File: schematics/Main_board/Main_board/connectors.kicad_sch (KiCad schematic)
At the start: 13 parts, among them J1 USB_B_Micro, J2 Conn_01x16_Female

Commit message: fix: 3d step file paths
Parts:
- D2, D3, D4: footprint Resistor_SMD:R_0603_1608Metric -> Resistor_SMD:R_0402_1005Metric
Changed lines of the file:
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@@
       (effects (font (size 1.27 1.27)) (justify left) hide)
     )
-    (property "Footprint" "Resistor_SMD:R_0603_1608Metric" (at 46.99 110.49 0)
+    (property "Footprint" "Resistor_SMD:R_0402_1005Metric" (at 46.99 110.49 0)
       (effects (font (size 1.27 1.27)) hide)
     )
@@
       (effects (font (size 1.27 1.27)) (justify left) hide)
     )
-    (property "Footprint" "Resistor_SMD:R_0603_1608Metric" (at 50.8 110.49 0)
+    (property "Footprint" "Resistor_SMD:R_0402_1005Metric" (at 50.8 110.49 0)
       (effects (font (size 1.27 1.27)) hide)
     )
@@
       (effects (font (size 1.27 1.27)) (justify left) hide)
     )
-    (property "Footprint" "Resistor_SMD:R_0603_1608Metric" (at 54.61 110.49 0)
-      (effects (font (size 1.27 1.27)) hide)
-    )
+    (property "Footprint" "Resistor_SMD:R_0402_1005Metric" (at 54.61 110.49 0)
+      (effects (font (size 1.27 1.27)) hide)
+    )

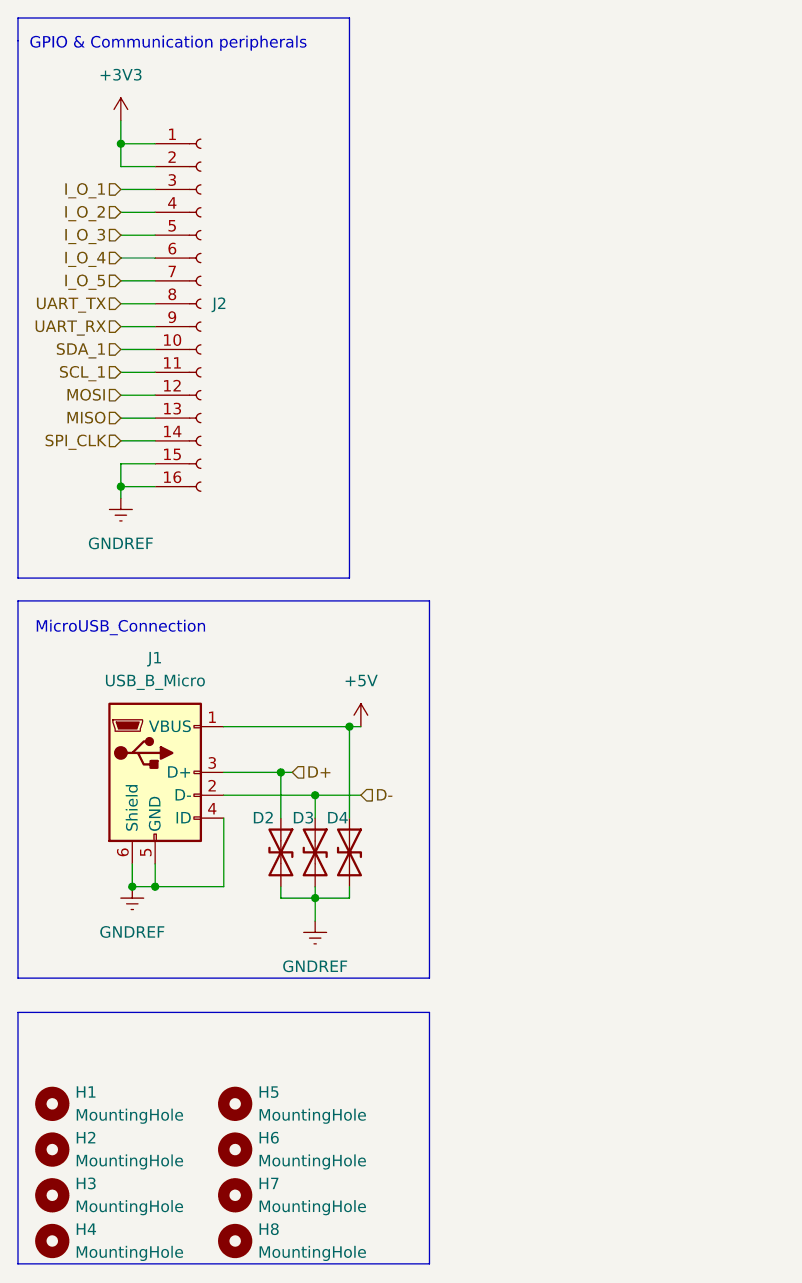
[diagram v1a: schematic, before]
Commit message: update: All the resistors and capacitors footprints changed from 0603 to 0402
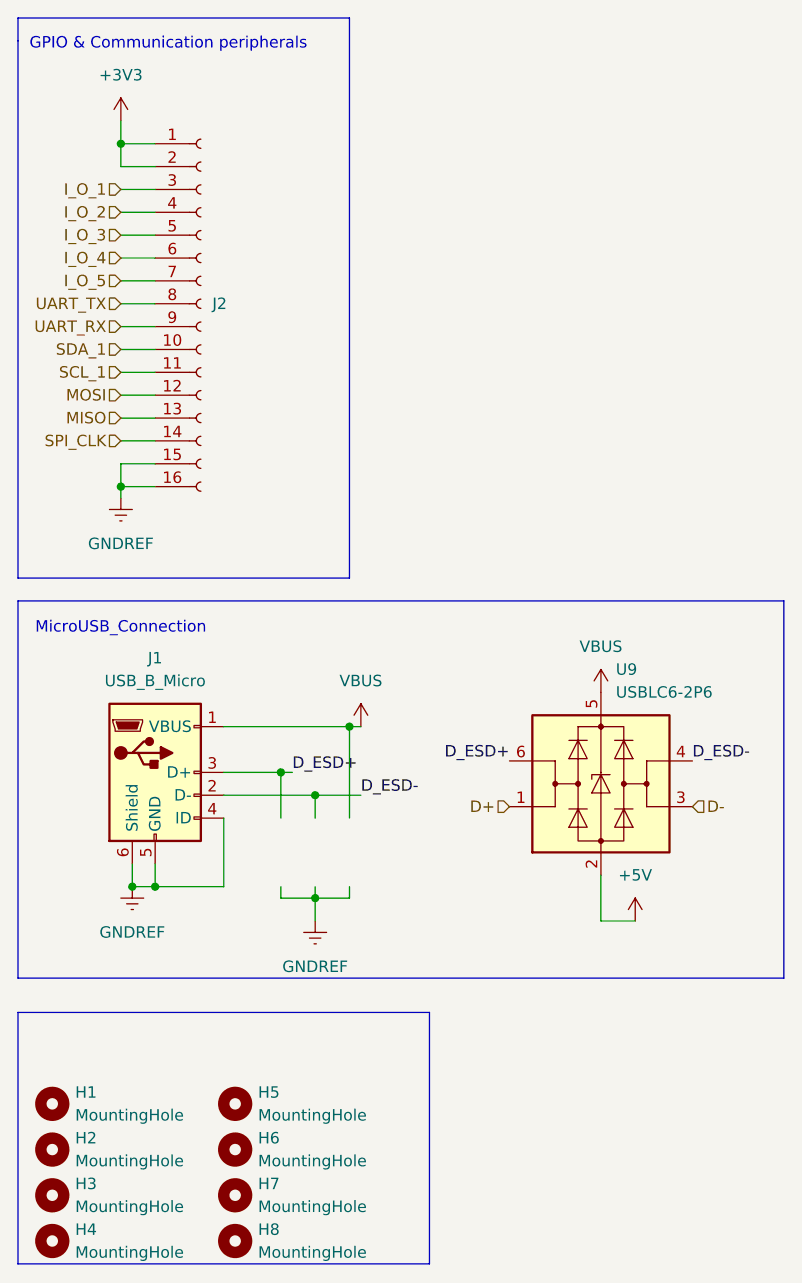
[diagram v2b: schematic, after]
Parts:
- removed D2, D3, D4: 0603ESDA-05N, Resistor_SMD:R_0402_1005Metric, symbol Device:D_TVS
- added U9: USBLC6-2P6, Package_TO_SOT_SMD:SOT-666, symbol Power_Protection:USBLC6-2P6
- J2: footprint Connector_PinSocket_2.54mm:PinSocket_1x16_P2.54mm_Horizontal -> Connector_FFC-FPC:TE_1-84953-6_1x16-1MP_P1.0mm_Horizontal; #LCSC Part re -> C13744
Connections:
- net +5V: now also U9.2 (GND); no longer J1.1 (VBUS)
- net D+: now also U9.1 (I/O1); no longer J1.3 (D+)
- net D-: now also U9.3 (I/O2); no longer J1.2 (D-)
- new net D_ESD+: J1.3 (D+), U9.6 (I/O1)
- new net D_ESD-: J1.2 (D-), U9.4 (I/O2)
- new net VBUS: J1.1 (VBUS), U9.5 (VBUS)
